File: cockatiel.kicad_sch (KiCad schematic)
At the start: 1 part

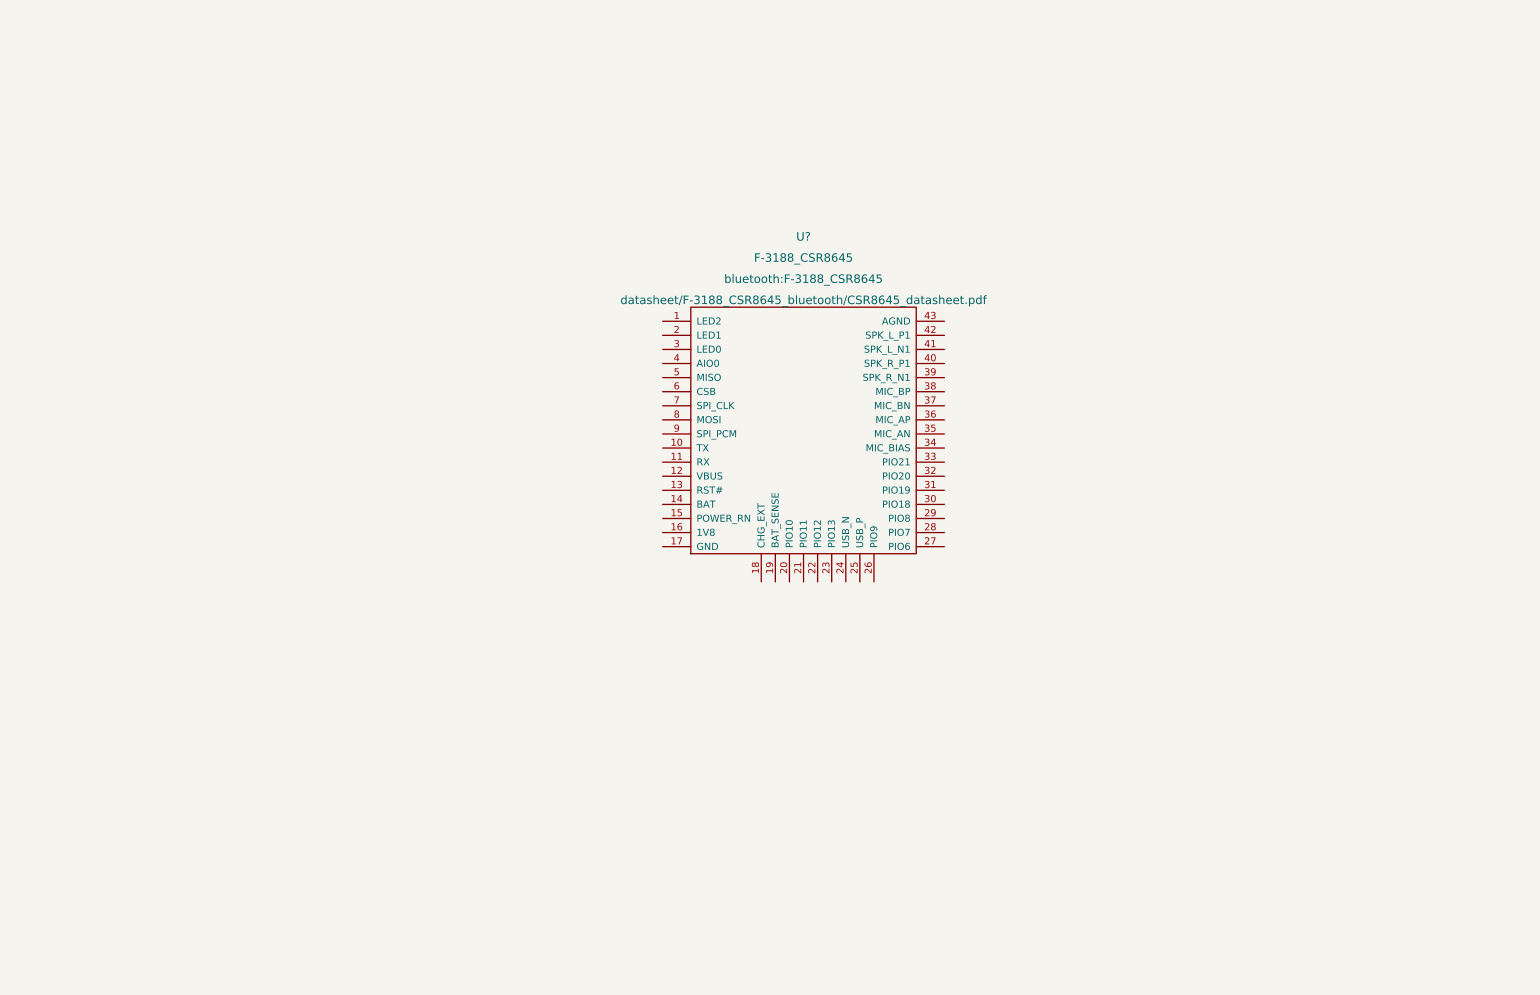
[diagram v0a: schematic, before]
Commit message: Add some power nets and labels for in-use pins
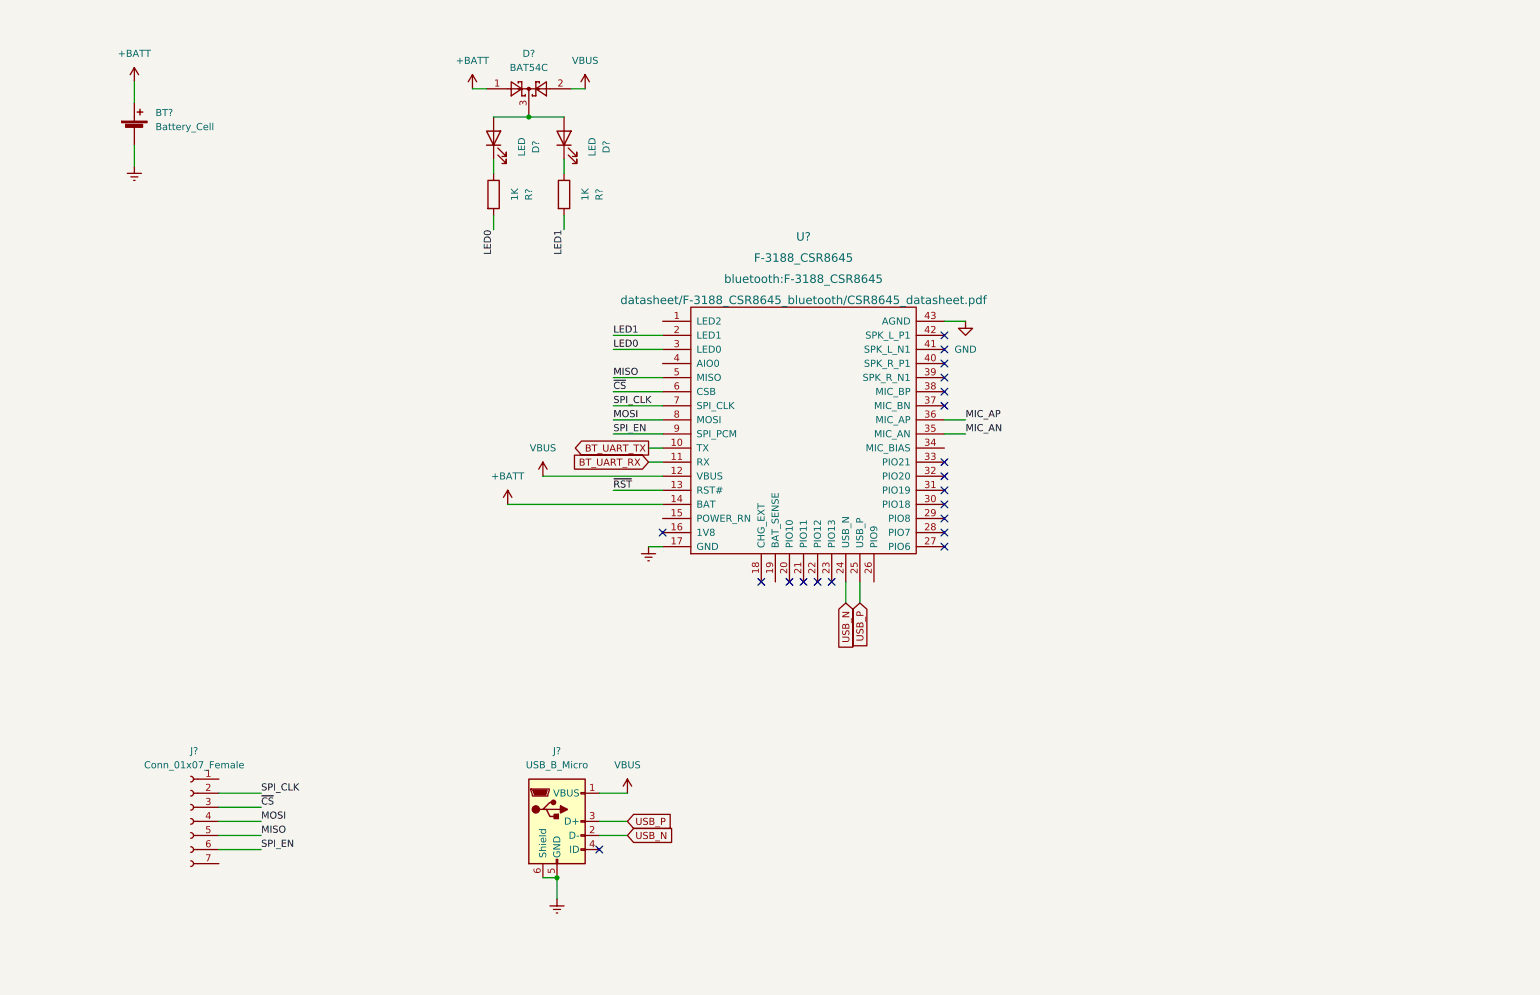
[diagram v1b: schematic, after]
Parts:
- added BT?: Battery_Cell, symbol Device:Battery_Cell
- added D?: BAT54C, Package_TO_SOT_SMD:SOT-23, symbol Diode:BAT54C
- added D? (x2): LED, LED_SMD:LED_0805_2012Metric_Pad1.15x1.40mm_HandSolder, symbol Device:LED
- added J?: Conn_01x07_Female, Connector_PinSocket_2.54mm:PinSocket_1x07_P2.54mm_Vertical, symbol Connector:Conn_01x07_Female
- added J?: USB_B_Micro, symbol Connector:USB_B_Micro
- added R? (x2): 1K, Resistor_SMD:R_0805_2012Metric_Pad1.20x1.40mm_HandSolder, symbol Device:R
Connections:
- net BT_UART_TX: now reaches U?.10 (TX)
- net BT_UART_RX: now reaches U?.11 (RX)
- net VBUS: now reaches U?.12 (VBUS)
- net VBUS: now also D?.2, J?.1 (VBUS)
- net ~{RST}: now reaches U?.13 (RST#)
- net +BATT: now reaches U?.14 (BAT)
- net +BATT: now also BT?.1 (+), D?.1
- net Earth: now reaches U?.17 (GND)
- net Earth: now also BT?.2 (-), J?.5 (GND), J?.6 (Shield)
- net LED1: now reaches U?.2 (LED1)
- net LED1: now also R?.2
- net USB_N: now reaches U?.24 (USB_N)
- net USB_N: now also J?.2 (D-)
- net USB_P: now reaches U?.25 (USB_P)
- net USB_P: now also J?.3 (D+)
- net LED0: now reaches U?.3 (LED0)
- net LED0: now also R?.2
- net MIC_AN: now reaches U?.35 (MIC_AN)
- net MIC_AP: now reaches U?.36 (MIC_AP)
- net GND: now reaches U?.43 (AGND)
- net MISO: now reaches U?.5 (MISO)
- net MISO: now also J?.5 (Pin_5)
- net ~{CS}: now reaches U?.6 (CSB)
- net ~{CS}: now also J?.3 (Pin_3)
- net SPI_CLK: now reaches U?.7 (SPI_CLK)
- net SPI_CLK: now also J?.2 (Pin_2)
- net MOSI: now reaches U?.8 (MOSI)
- net MOSI: now also J?.4 (Pin_4)
- net SPI_EN: now reaches U?.9 (SPI_PCM)
- net SPI_EN: now also J?.6 (Pin_6)
- new net: D?.2 (A), D?.2 (A), D?.3
- new net: D?.1 (K), R?.1 (x2)
- no-connect marks 0 -> 20

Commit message: WIP check-in
1. Add audio inputs via a TRRS socket (smartphone-style headset).
2. Add audio passthrough via a second socket.
3. Support sending audio out on 3.5mm socket headset input.
4. Add headers for cox's microphone input, and output. This uses
   0.1" pitch headers for now.
5. Support bypaassing the isolation transformer during development.
6. Support USB via 0.1" header e.g. if using a panel-mounted USB connector.
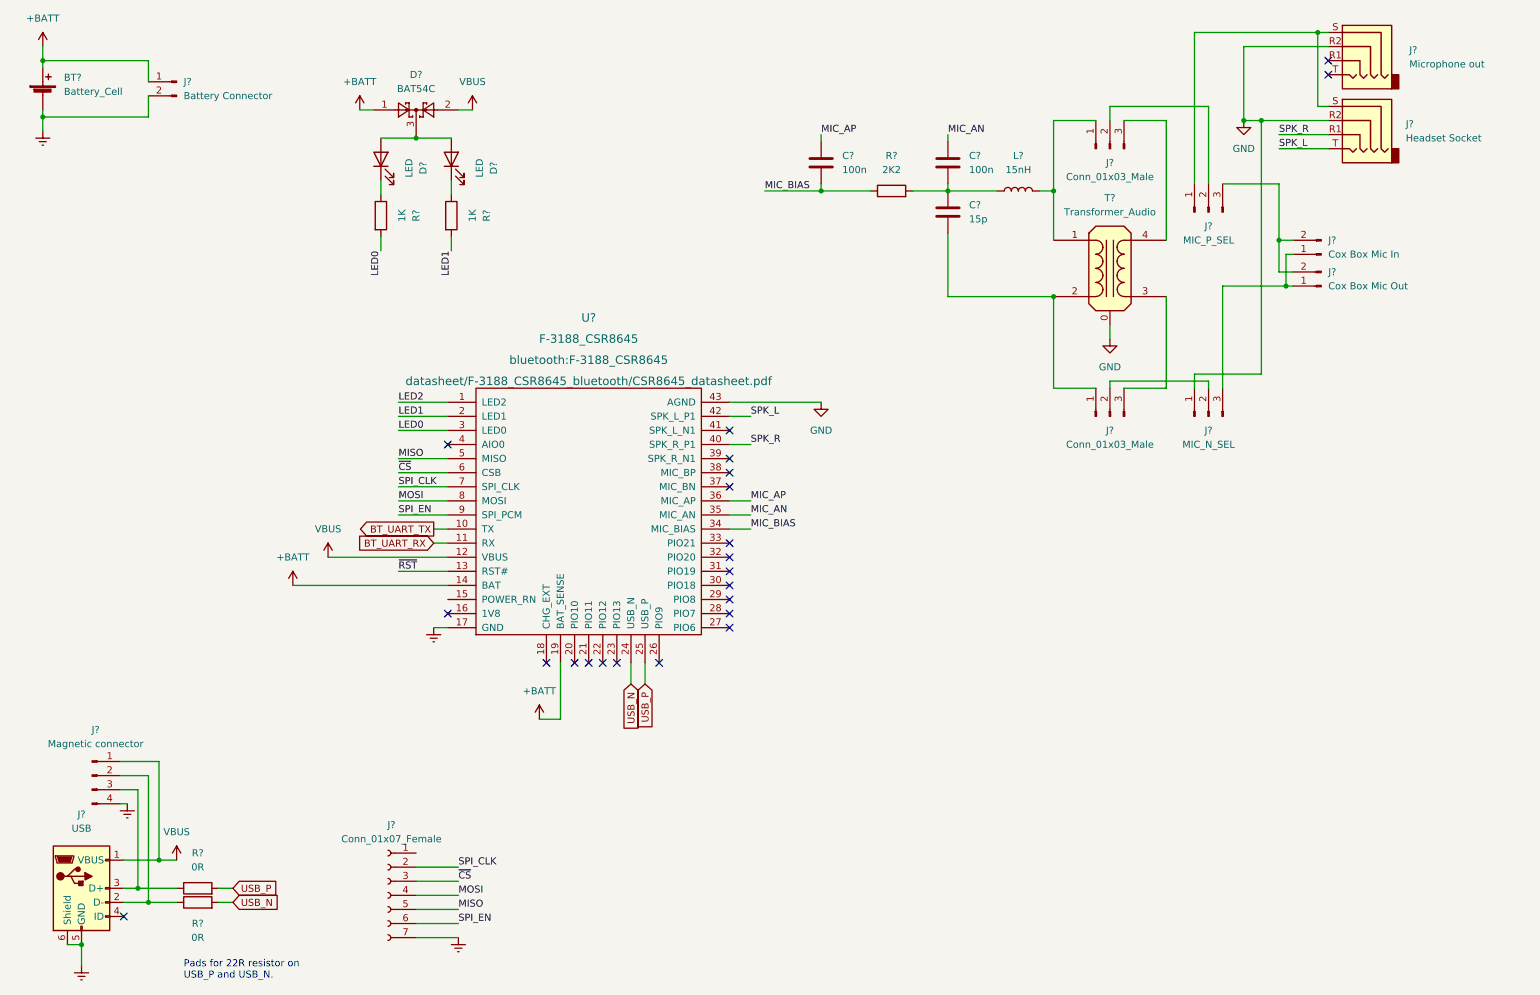
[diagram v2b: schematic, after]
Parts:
- added C? (x2): 100n, symbol Device:C
- added C?: 15p, symbol Device:C
- added J? (x2): Conn_01x03_Male, Connector_PinHeader_2.54mm:PinHeader_1x03_P2.54mm_Vertical, symbol Connector:Conn_01x03_Male
- added J?: Cox Box Mic In, Connector_PinHeader_2.54mm:PinHeader_1x02_P2.54mm_Vertical, symbol Connector:Conn_01x02_Male
- added J?: MIC_N_SEL, Connector_PinHeader_2.54mm:PinHeader_1x03_P2.54mm_Vertical, symbol Connector:Conn_01x03_Male
- added J?: Magnetic connector, symbol Connector:Conn_01x04_Male
- added J?: Headset Socket, Connector_Audio:Jack_3.5mm_CUI_SJ-3524-SMT_Horizontal, symbol Connector:AudioJack4
- added J?: Battery Connector, Connector_JST:JST_PH_S2B-PH-K_1x02_P2.00mm_Horizontal, symbol Connector:Conn_01x02_Male
- added J?: MIC_P_SEL, Connector_PinHeader_2.54mm:PinHeader_1x03_P2.54mm_Vertical, symbol Connector:Conn_01x03_Male
- added J?: Microphone out, Connector_Audio:Jack_3.5mm_CUI_SJ-3524-SMT_Horizontal, symbol Connector:AudioJack4
- added J?: Cox Box Mic Out, Connector_PinHeader_2.54mm:PinHeader_1x02_P2.54mm_Vertical, symbol Connector:Conn_01x02_Male
- added L?: 15nH, Inductor_SMD:L_0805_2012Metric_Pad1.05x1.20mm_HandSolder, symbol Device:L
- added R?: 2K2, Resistor_SMD:R_0805_2012Metric_Pad1.20x1.40mm_HandSolder, symbol Device:R
- added R? (x2): 0R, Resistor_SMD:R_0805_2012Metric_Pad1.20x1.40mm_HandSolder, symbol Device:R
- added T?: Transformer_Audio, symbol Device:Transformer_Audio
- J?: value USB_B_Micro -> USB
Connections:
- net +BATT: now also U?.19 (BAT_SENSE), J?.1 (Pin_1)
- net Earth: now also J?.7 (Pin_7), J?.2 (Pin_2), J?.4 (Pin_4)
- net GND: now also J?.1 (Pin_1), J?.R2, J?.R2, T?.0
- net MIC_AN: now also C?.1
- net MIC_AP: now also C?.1
- net USB_N: now also R?.2; no longer J?.2 (D-)
- net USB_P: now also R?.2; no longer J?.3 (D+)
- net VBUS: now also J?.1 (Pin_1)
- net LED2: now reaches U?.1 (LED2)
- net MIC_BIAS: now reaches U?.34 (MIC_BIAS)
- net MIC_BIAS: now also C?.2, R?.1
- net SPK_R: now reaches U?.40 (SPK_R_P1)
- net SPK_R: now also J?.R1
- net SPK_L: now reaches U?.42 (SPK_L_P1)
- net SPK_L: now also J?.T
- new net: C?.1, C?.2, L?.1, R?.2
- new net: C?.2, J?.1 (Pin_1), T?.2 (AB)
- new net: J?.2 (Pin_2), J?.2 (Pin_2) (x2)
- new net: J?.3 (Pin_3), T?.3 (SA)
- new net: J?.1 (Pin_1), J?.1 (Pin_1), J?.3 (Pin_3)
- new net: J?.2 (Pin_2), J?.2 (Pin_2), J?.3 (Pin_3)
- new net: J?.1 (Pin_1), L?.2, T?.1 (AA)
- new net: J?.3 (Pin_3), T?.4 (SB)
- new net: J?.3 (D+), J?.3 (Pin_3), R?.1
- new net: J?.2 (D-), J?.2 (Pin_2), R?.1
- new net: J?.1 (Pin_1), J?.S, J?.S
- no-connect marks 20 -> 22
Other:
- note added: "Pads for 22R resistor on USB_P and USB_N."
- moved on the sheet: BT?, D?, J?, R?, U?

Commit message: Expose all the PIOs on a debug header.
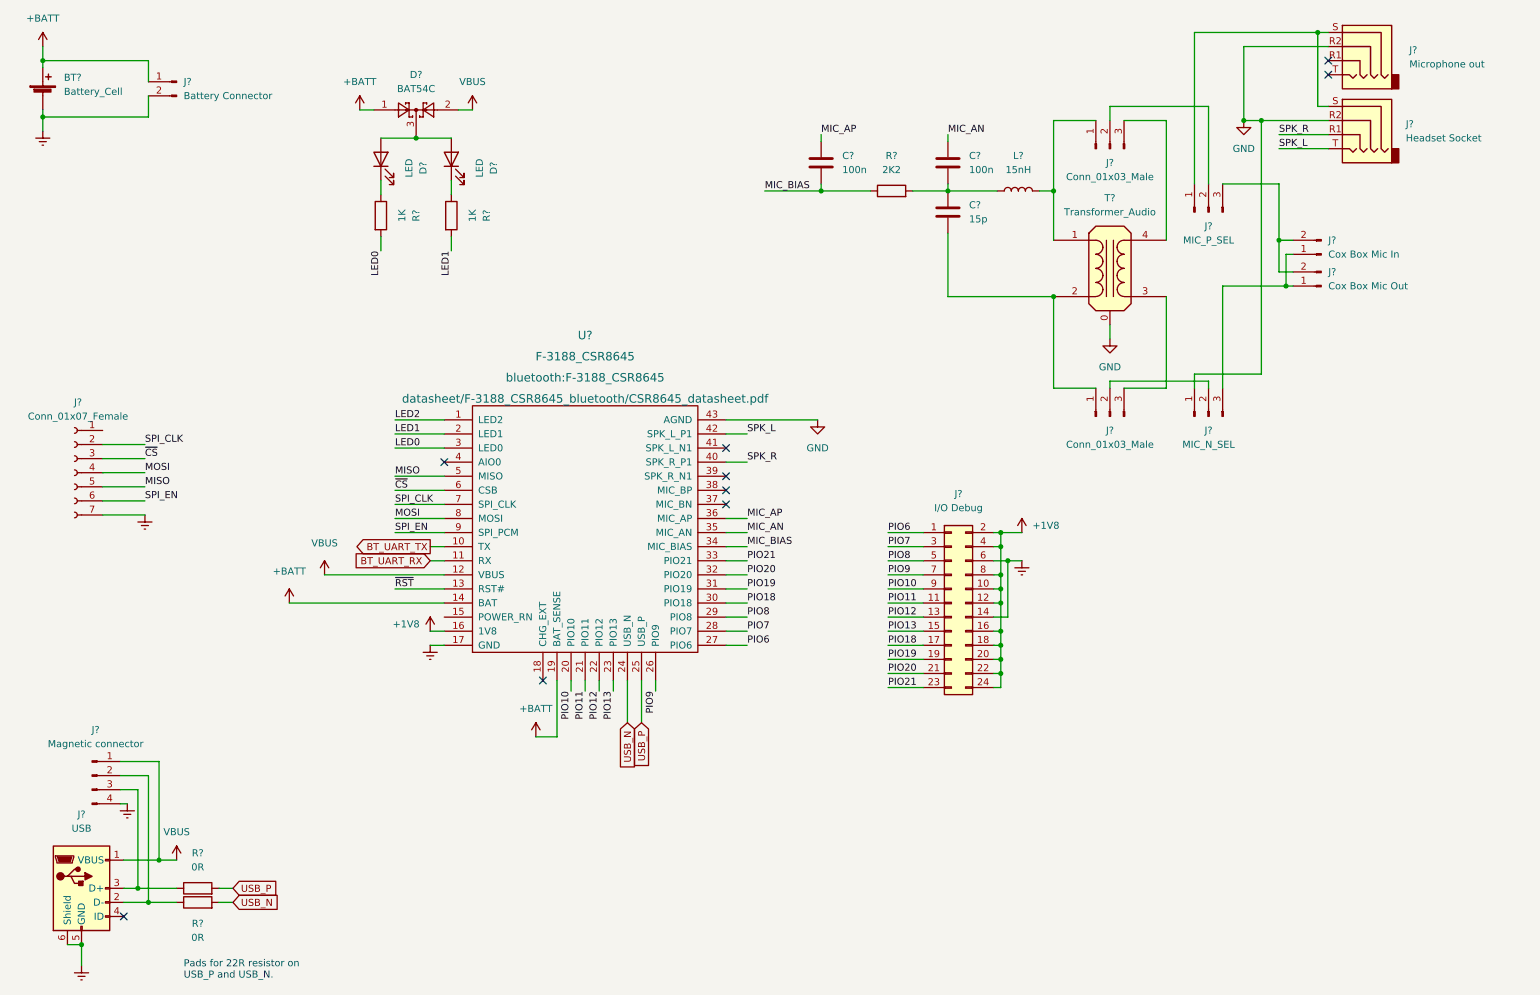
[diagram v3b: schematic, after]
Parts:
- added J?: I/O Debug, Connector_PinHeader_2.54mm:PinHeader_2x07_P2.54mm_Vertical, symbol Connector_Generic:Conn_02x12_Odd_Even
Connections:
- net Earth: now also J?.14 (Pin_14), J?.6 (Pin_6)
- net +1V8: now reaches U?.16 (1V8)
- net +1V8: now also J?.10 (Pin_10), J?.12 (Pin_12), J?.16 (Pin_16), J?.18 (Pin_18), J?.2 (Pin_2), J?.20 (Pin_20), J?.22 (Pin_22), J?.24 (Pin_24), J?.4 (Pin_4), J?.8 (Pin_8)
- net PIO10: now reaches U?.20 (PIO10)
- net PIO10: now also J?.9 (Pin_9)
- net PIO11: now reaches U?.21 (PIO11)
- net PIO11: now also J?.11 (Pin_11)
- net PIO12: now reaches U?.22 (PIO12)
- net PIO12: now also J?.13 (Pin_13)
- net PIO13: now reaches U?.23 (PIO13)
- net PIO13: now also J?.15 (Pin_15)
- net PIO9: now reaches U?.26 (PIO9)
- net PIO9: now also J?.7 (Pin_7)
- net PIO6: now reaches U?.27 (PIO6)
- net PIO6: now also J?.1 (Pin_1)
- net PIO7: now reaches U?.28 (PIO7)
- net PIO7: now also J?.3 (Pin_3)
- net PIO8: now reaches U?.29 (PIO8)
- net PIO8: now also J?.5 (Pin_5)
- net PIO18: now reaches U?.30 (PIO18)
- net PIO18: now also J?.17 (Pin_17)
- net PIO19: now reaches U?.31 (PIO19)
- net PIO19: now also J?.19 (Pin_19)
- net PIO20: now reaches U?.32 (PIO20)
- net PIO20: now also J?.21 (Pin_21)
- net PIO21: now reaches U?.33 (PIO21)
- net PIO21: now also J?.23 (Pin_23)
- no-connect marks 22 -> 9
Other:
- moved on the sheet: J?, U?
